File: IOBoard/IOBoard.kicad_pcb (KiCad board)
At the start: 2 copper layers, 65 x 30 mm, 20 parts, among them J2 USB_A, J4 USB_C_Receptacle_USB2.0_14P, J6 USB_C_Receptacle_USB2.0_14P

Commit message: optimize pcb (yesterday)
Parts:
- moved C6 10.9 mm to (168.0, 97.2)
- moved C7 10.9 mm to (168.0, 98.8)
- moved USB1 5.05 mm to (174.8, 101.5)
- moved D1 1.95 mm to (157.2, 97.8)
- moved C1 1.59 mm to (164.0, 98.5)
- moved J2 1.18 mm to (161.0, 103.8)
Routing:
- net Net-(U1-DP2): track 42.2 -> 31.6 mm, vias 2 -> 0
- net GND: track 171.4 -> 161.4 mm, vias 11 -> 15
- net VCC: track 140.5 -> 131.5 mm, vias 8 -> 9
- net Net-(U1-DP1): track 30.3 -> 24.7 mm
- net Net-(U1-DM1): track 31.4 -> 26.1 mm
- net Net-(U1-DM2): track 40.9 -> 36.7 mm
- net Net-(J2-D-): track 13.4 -> 12.2 mm
- net Net-(D1-A): track 10.8 -> 10.7 mm, vias 1 -> 2

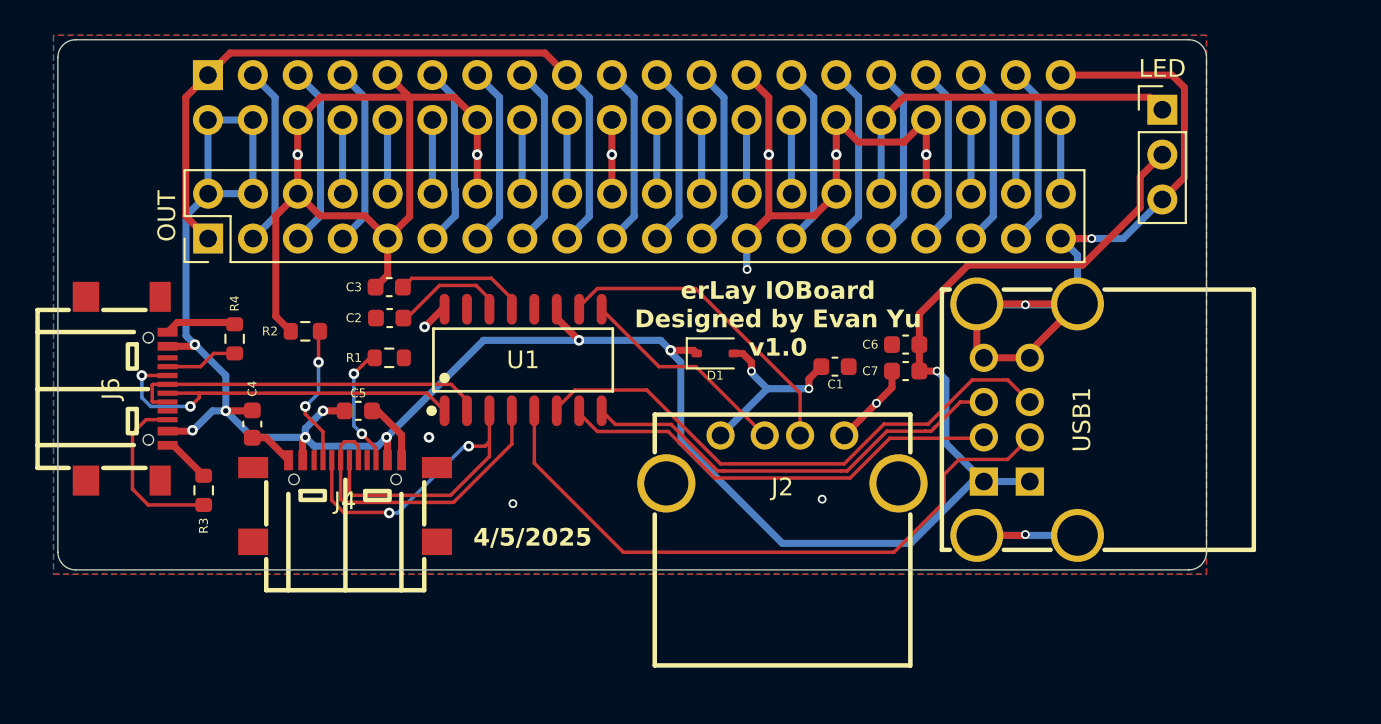
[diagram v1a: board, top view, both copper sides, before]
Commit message: Update IOBoard usb c connectors
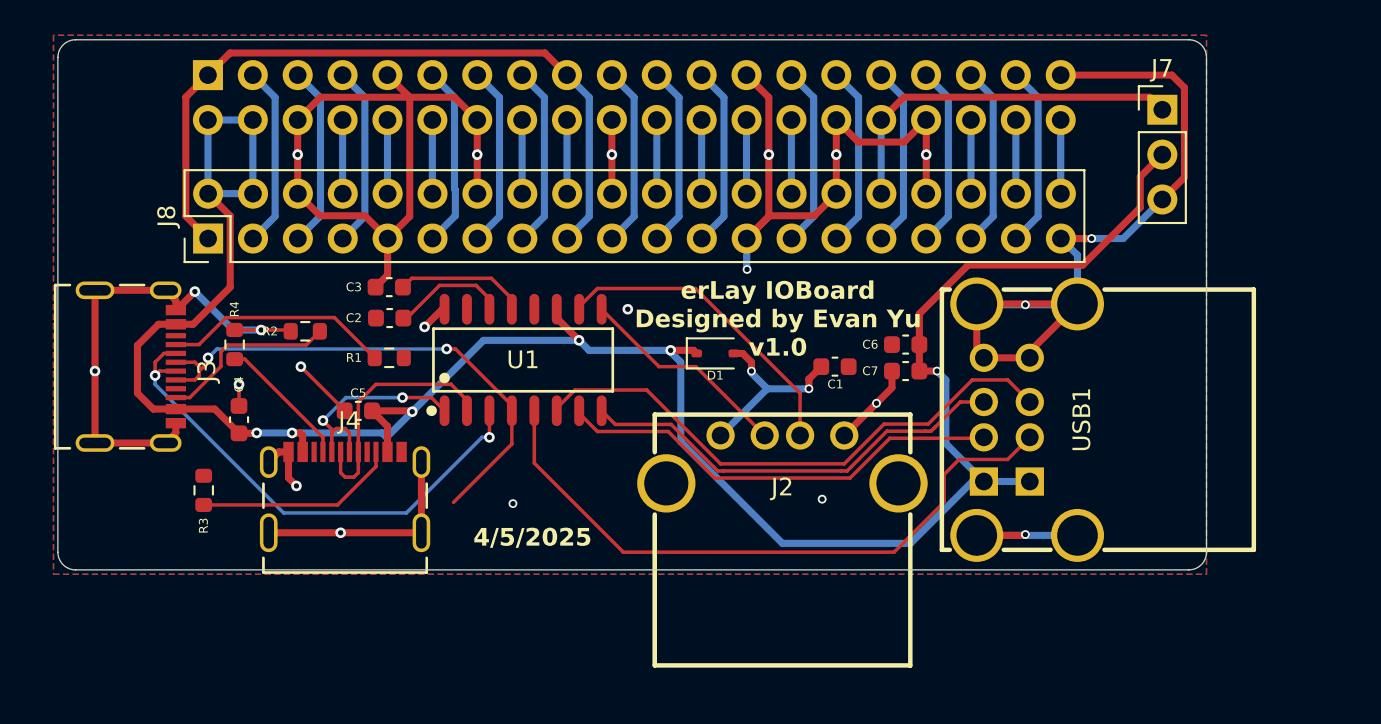
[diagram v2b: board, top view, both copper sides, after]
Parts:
- removed J6: USB_C_Receptacle_USB2.0_14P, Components:USB-TYPE-C-SMD_TYPE-C-16P-QTWT
- added J3: 2171790001, Components:MOLEX_2171790001, F.Cu at (123.2, 98.5)
- J4: value USB_C_Receptacle_USB2.0_14P -> 2171790001; footprint Components:USB-TYPE-C-SMD_TYPE-C-16P-QTWT -> Components:MOLEX_2171790001
- moved C4 0.79 mm to (130.2, 101.5)
- moved J4 0.65 mm to (136.2, 106.8)
- moved R4 0.33 mm to (130.0, 97.2)
- renumbered IN to J1, LED to J7, OUT to J8
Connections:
- C4 pad 1: VCC -> GND
- C4 pad 2: GND -> VCC
- C5 pad 1: VCC -> GND
- C5 pad 2: GND -> VCC
- J4 pad A6: Net-(U1-DP3) -> Net-(J4-DP1)
- J4 pad A7: Net-(U1-DM3) -> Net-(J4-DN1)
- J4 pad A8: (no net) -> unconnected-(J4-SBU1-PadA8)
- J4 pad B6: Net-(U1-DP3) -> Net-(J4-DP1)
- J4 pad B7: Net-(U1-DM3) -> Net-(J4-DN1)
- J4 pad B8: (no net) -> unconnected-(J4-SBU2-PadB8)
- R1 pad 1: Net-(J4-CC2) -> Net-(J3-CC1)
- R2 pad 1: Net-(J4-CC1) -> Net-(J3-CC2)
- R3 pad 1: Net-(J6-CC2) -> Net-(J4-CC2)
- R4 pad 1: Net-(J6-CC1) -> Net-(J4-CC1)
- U1 pad 1: Net-(U1-DM4) -> Net-(J4-DN1)
- U1 pad 2: Net-(U1-DP4) -> Net-(J4-DP1)
- U1 pad 3: Net-(U1-DM3) -> Net-(J3-DN1)
- U1 pad 4: Net-(U1-DP3) -> Net-(J3-DP1)
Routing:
- net Net-(J3-DP1): track 0.00 -> 29.9 mm, vias 0 -> 2
- net Net-(J3-DN1): track 0.00 -> 29.1 mm, vias 0 -> 2
- net GND: track 161.4 -> 189.3 mm, vias 15 -> 22
- net Net-(U1-DM3): track 26.5 -> 0.00 mm, vias 2 -> 0
- net Net-(U1-DM4): track 22.7 -> 0.00 mm, vias 2 -> 0
- net Net-(U1-DP4): track 20.6 -> 0.00 mm
- net Net-(U1-DP3): track 18.0 -> 0.00 mm
- net Net-(J4-DP1): track 0.00 -> 13.9 mm
- net Net-(J3-CC1): track 0.00 -> 12.8 mm
- net Net-(J4-DN1): track 0.00 -> 12.0 mm, vias 0 -> 2
- net Net-(J3-CC2): track 0.00 -> 10.2 mm
- net Net-(J6-CC2): track 9.87 -> 0.00 mm
- net Net-(J4-CC2): track 6.96 -> 11.5 mm, vias 2 -> 0
- net Net-(J6-CC1): track 4.10 -> 0.00 mm
- net VCC: track 131.5 -> 132.0 mm, vias 9 -> 6
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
